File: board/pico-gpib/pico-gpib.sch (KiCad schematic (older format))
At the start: 37 parts, among them J2 USB_B_Micro, J3 RPI_GPIO, J4 Debug, U1 RP2040, U4 W25Q128JVS, U5 NCP1117-3.3, U6 CAT24C32, Y1 12M10PI/XT324-10/20

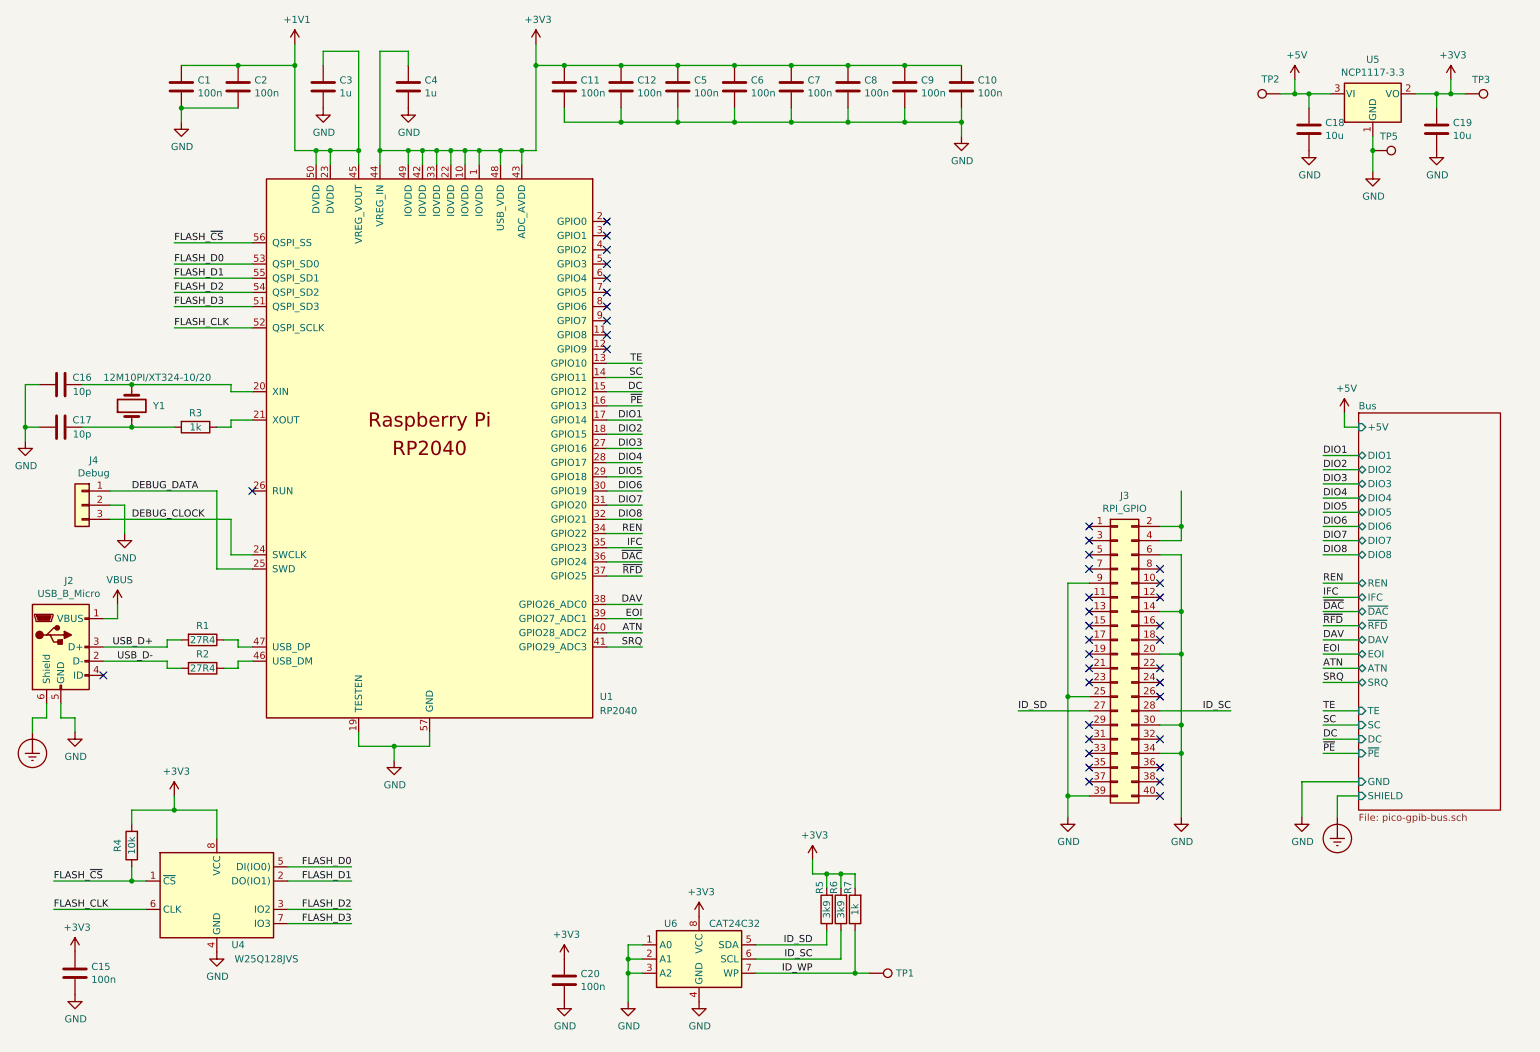
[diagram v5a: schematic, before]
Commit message: Renumber caps to make more sense.
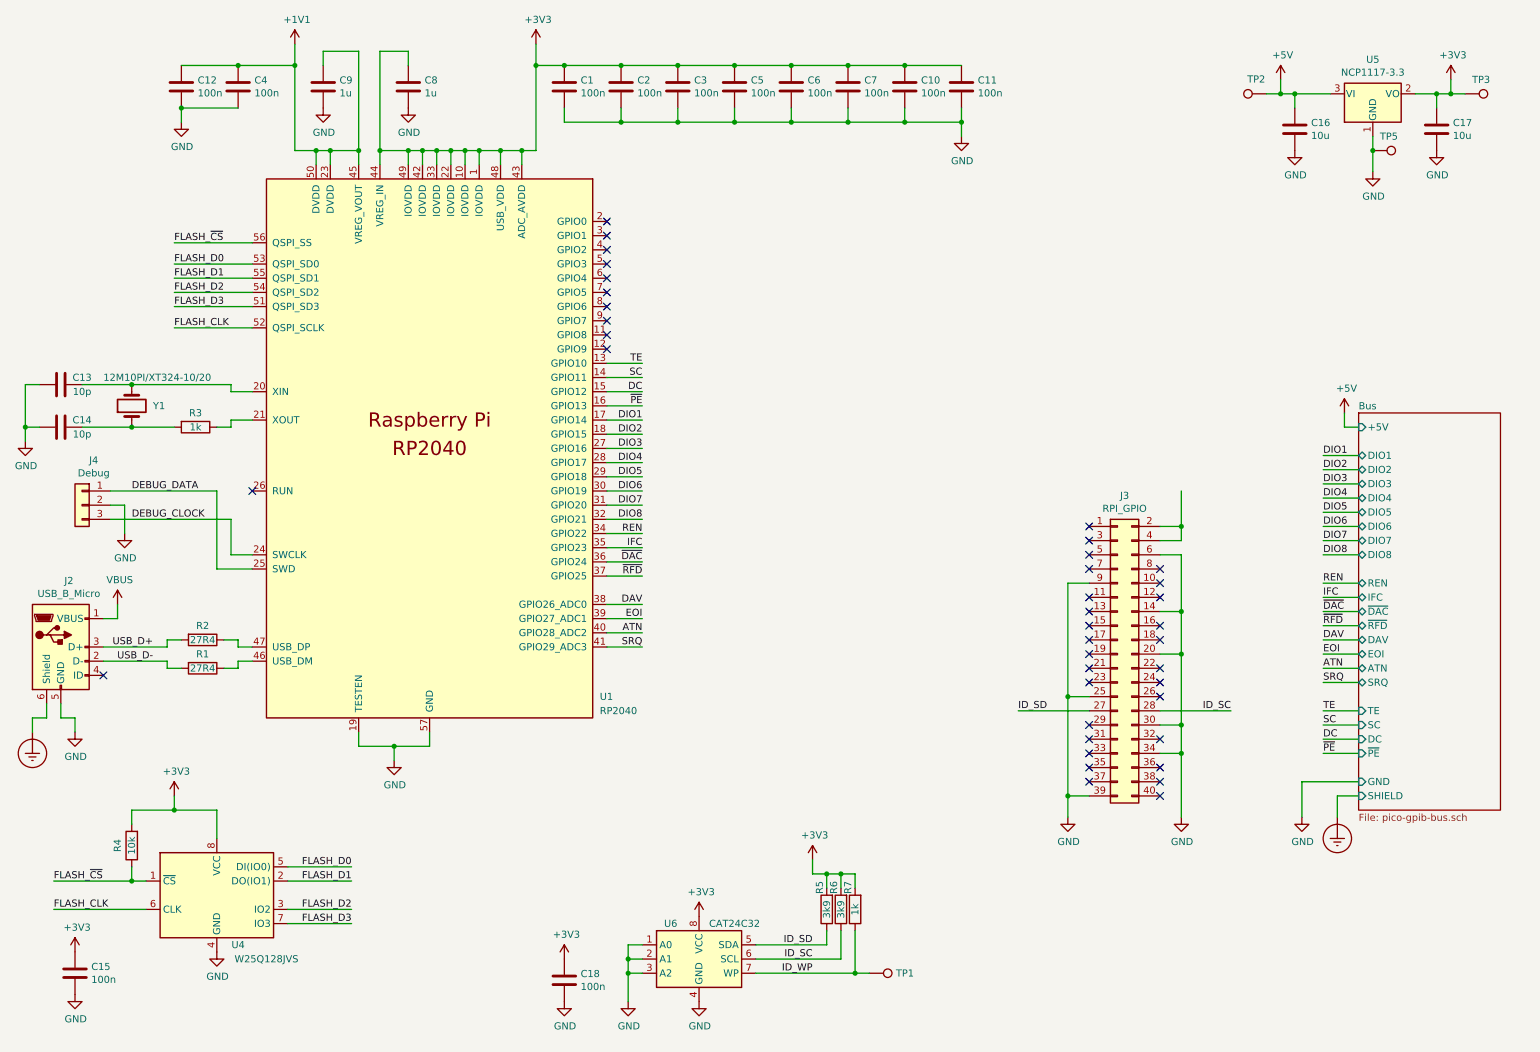
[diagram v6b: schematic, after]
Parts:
- renumbered C10 to C1, C6 to C10, C5 to C11, C1 to C12, C16 to C13, C17 to C14, C18 to C16, C19 to C17, C20 to C18, C8 to C2, C9 to C3, C2 to C4, C11 to C5, C12 to C6, C4 to C8, C3 to C9, R2 to R1, R1 to R2
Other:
- moved on the sheet: C1, C10, C11, C16, C2, C3, C5, C6, C7, TP2
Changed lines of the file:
@@
 ~PE
 $Comp
-L Device:C C4
+L Device:C C8
 U 1 1 625CDD18
 P 3300 1050
-F 0 "C4" H 3415 1096 50  0000 L CNN
+F 0 "C8" H 3415 1096 50  0000 L CNN
 F 1 "1u" H 3415 1005 50  0000 L CNN
 F 2 "Capacitor_SMD:C_0402_1005Metric" H 3338 900 50  0001 C CNN
@@
 $EndComp
 $Comp
-L Device:C C5
+L Device:C C11
 U 1 1 625CFFE4
-P 5200 1050
-F 0 "C5" H 5315 1096 50  0000 L CNN
-F 1 "100n" H 5315 1005 50  0000 L CNN
-F 2 "Capacitor_SMD:C_0402_1005Metric" H 5238 900 50  0001 C CNN
-F 3 "~" H 5200 1050 50  0001 C CNN
-	1    5200 1050
-	1    0    0    -1
-$EndComp
-$Comp
-L Device:C C6
+P 7200 1050
+F 0 "C11" H 7315 1096 50  0000 L CNN
+F 1 "100n" H 7315 1005 50  0000 L CNN
+F 2 "Capacitor_SMD:C_0402_1005Metric" H 7238 900 50  0001 C CNN
+F 3 "~" H 7200 1050 50  0001 C CNN
+	1    7200 1050
+	1    0    0    -1
+$EndComp
+$Comp
+L Device:C C10
 U 1 1 625D0C85
-P 5600 1050
-F 0 "C6" H 5715 1096 50  0000 L CNN
-F 1 "100n" H 5715 1005 50  0000 L CNN
-F 2 "Capacitor_SMD:C_0402_1005Metric" H 5638 900 50  0001 C CNN
-F 3 "~" H 5600 1050 50  0001 C CNN
-	1    5600 1050
-	1    0    0    -1
-$EndComp
-$Comp
-L Device:C C7
-U 1 1 625D1419
-P 6000 1050
-F 0 "C7" H 6115 1096 50  0000 L CNN
-F 1 "100n" H 6115 1005 50  0000 L CNN
-F 2 "Capacitor_SMD:C_0402_1005Metric" H 6038 900 50  0001 C CNN
-F 3 "~" H 6000 1050 50  0001 C CNN
-	1    6000 1050
-	1    0    0    -1
-$EndComp
-$Comp
-L Device:C C8
-U 1 1 625D1CD7
-P 6400 1050
-F 0 "C8" H 6515 1096 50  0000 L CNN
-F 1 "100n" H 6515 1005 50  0000 L CNN
-F 2 "Capacitor_SMD:C_0402_1005Metric" H 6438 900 50  0001 C CNN
-F 3 "~" H 6400 1050 50  0001 C CNN
-	1    6400 1050
-	1    0    0    -1
-$EndComp
-$Comp
-L Device:C C9
-U 1 1 625D225C
 P 6800 1050
-F 0 "C9" H 6915 1096 50  0000 L CNN
+F 0 "C10" H 6915 1096 50  0000 L CNN
 F 1 "100n" H 6915 1005 50  0000 L CNN
 F 2 "Capacitor_SMD:C_0402_1005Metric" H 6838 900 50  0001 C CNN
@@
 $EndComp
 $Comp
-L Device:C C10
+L Device:C C1
 U 1 1 625D27B5
-P 7200 1050
-F 0 "C10" H 7315 1096 50  0000 L CNN
-F 1 "100n" H 7315 1005 50  0000 L CNN
-F 2 "Capacitor_SMD:C_0402_1005Metric" H 7238 900 50  0001 C CNN
-F 3 "~" H 7200 1050 50  0001 C CNN
-	1    7200 1050
+P 4400 1050
+F 0 "C1" H 4515 1096 50  0000 L CNN
+F 1 "100n" H 4515 1005 50  0000 L CNN
+F 2 "Capacitor_SMD:C_0402_1005Metric" H 4438 900 50  0001 C CNN
+F 3 "~" H 4400 1050 50  0001 C CNN
+	1    4400 1050
 	1    0    0    -1
 $EndComp
@@
 $EndComp
 $Comp
-L Device:C C3
+L Device:C C9
 U 1 1 625F6CF0
 P 2700 1050
-F 0 "C3" H 2815 1096 50  0000 L CNN
+F 0 "C9" H 2815 1096 50  0000 L CNN
 F 1 "1u" H 2815 1005 50  0000 L CNN
 F 2 "Capacitor_SMD:C_0402_1005Metric" H 2738 900 50  0001 C CNN
@@
 $EndComp
 $Comp
-L Device:C C2
-U 1 1 625F79B4
-P 2100 1050
-F 0 "C2" H 2215 1096 50  0000 L CNN
-F 1 "100n" H 2215 1005 50  0000 L CNN
-F 2 "Capacitor_SMD:C_0402_1005Metric" H 2138 900 50  0001 C CNN
-F 3 "~" H 2100 1050 50  0001 C CNN
-	1    2100 1050
-	1    0    0    -1
-$EndComp
-$Comp
-L Device:C C1
+L Device:C C12
 U 1 1 625F8A02
 P 1700 1050
-F 0 "C1" H 1815 1096 50  0000 L CNN
+F 0 "C12" H 1815 1096 50  0000 L CNN
 F 1 "100n" H 1815 1005 50  0000 L CNN
 F 2 "Capacitor_SMD:C_0402_1005Metric" H 1738 900 50  0001 C CNN
@@
 $EndComp
 $Comp
-L Device:R R1
+L Device:R R2
 U 1 1 626338A8
 P 1850 4950
-F 0 "R1" V 1750 4950 50  0000 C CNN
+F 0 "R2" V 1750 4950 50  0000 C CNN
 F 1 "27R4" V 1850 4950 50  0000 C CNN
 F 2 "Resistor_SMD:R_0402_1005Metric" V 1780 4950 50  0001 C CNN
@@
 $EndComp
 $Comp
-L Device:R R2
+L Device:R R1
 U 1 1 62638F62
 P 1850 5150
-F 0 "R2" V 1750 5150 50  0000 C CNN
+F 0 "R1" V 1750 5150 50  0000 C CNN
 F 1 "27R4" V 1850 5150 50  0000 C CNN
 F 2 "Resistor_SMD:R_0402_1005Metric" V 1780 5150 50  0001 C CNN
@@
 Wire Wire Line
 	2100 900  2500 900
-$Comp
-L Device:C C12
-U 1 1 626DDD7A
-P 4800 1050
-F 0 "C12" H 4915 1096 50  0000 L CNN
-F 1 "100n" H 4915 1005 50  0000 L CNN
-F 2 "Capacitor_SMD:C_0402_1005Metric" H 4838 900 50  0001 C CNN
-F 3 "~" H 4800 1050 50  0001 C CNN
-	1    4800 1050
-	1    0    0    -1
-$EndComp
 Connection ~ 4800 900
 Wire Wire Line
 	4800 900  5200 900
-$Comp
-L Device:C C11
-U 1 1 626E7663
-P 4400 1050
-F 0 "C11" H 4515 1096 50  0000 L CNN
-F 1 "100n" H 4515 1005 50  0000 L CNN
-F 2 "Capacitor_SMD:C_0402_1005Metric" H 4438 900 50  0001 C CNN
-F 3 "~" H 4400 1050 50  0001 C CNN
-	1    4400 1050
-	1    0    0    -1
-$EndComp
 Connection ~ 4400 900
 Wire Wire Line
@@
 L power:GND #PWR0122
 U 1 1 628CC205
-P 9650 1500
-F 0 "#PWR0122" H 9650 1250 50  0001 C CNN
-F 1 "GND" H 9655 1327 50  0000 C CNN
-F 2 "" H 9650 1500 50  0001 C CNN
-F 3 "" H 9650 1500 50  0001 C CNN
-	1    9650 1500
-	1    0    0    -1
-$EndComp
-$Comp
-L Device:C C19
+P 9550 1500
+F 0 "#PWR0122" H 9550 1250 50  0001 C CNN
+F 1 "GND" H 9555 1327 50  0000 C CNN
+F 2 "" H 9550 1500 50  0001 C CNN
+F 3 "" H 9550 1500 50  0001 C CNN
+	1    9550 1500
+	1    0    0    -1
+$EndComp
+$Comp
+L Device:C C17
 U 1 1 628CC8FF
 P 10550 1350
-F 0 "C19" H 10665 1396 50  0000 L CNN
+F 0 "C17" H 10665 1396 50  0000 L CNN
 F 1 "10u" H 10665 1305 50  0000 L CNN
 F 2 "Capacitor_SMD:C_0402_1005Metric" H 10588 1200 50  0001 C CNN
@@
 $EndComp
 $Comp
-L Device:C C18
+L Device:C C16
 U 1 1 628CD260
-P 9650 1350
-F 0 "C18" H 9765 1396 50  0000 L CNN
-F 1 "10u" H 9765 1305 50  0000 L CNN
-F 2 "Capacitor_SMD:C_0402_1005Metric" H 9688 1200 50  0001 C CNN
-F 3 "~" H 9650 1350 50  0001 C CNN
-	1    9650 1350
+P 9550 1350
+F 0 "C16" H 9665 1396 50  0000 L CNN
+F 1 "10u" H 9665 1305 50  0000 L CNN
+F 2 "Capacitor_SMD:C_0402_1005Metric" H 9588 1200 50  0001 C CNN
+F 3 "~" H 9550 1350 50  0001 C CNN
+	1    9550 1350
 	1    0    0    -1
 $EndComp
@@
 	10550 1100 10550 1200
 Wire Wire Line
-	9800 1100 9650 1100
-Wire Wire Line
-	9650 1100 9650 1200
-Wire Wire Line
-	10100 1400 10100 1500
+	9800 1100 9550 1100
+Wire Wire Line
+	9550 1100 9550 1200
 $Comp
 L power:+3V3 #PWR0123
@@
 L power:+5V #PWR0124
 U 1 1 628F5D99
-P 9550 1000
-F 0 "#PWR0124" H 9550 850 50  0001 C CNN
-F 1 "+5V" H 9565 1173 50  0000 C CNN
-F 2 "" H 9550 1000 50  0001 C CNN
-F 3 "" H 9550 1000 50  0001 C CNN
-	1    9550 1000
-	1    0    0    -1
-$EndComp
-Wire Wire Line
-	9550 1000 9550 1100
-Wire Wire Line
-	9550 1100 9650 1100
-Connection ~ 9650 1100
+P 9450 1000
+F 0 "#PWR0124" H 9450 850 50  0001 C CNN
+F 1 "+5V" H 9465 1173 50  0000 C CNN
+F 2 "" H 9450 1000 50  0001 C CNN
+F 3 "" H 9450 1000 50  0001 C CNN
+	1    9450 1000
+	1    0    0    -1
+$EndComp
+Wire Wire Line
+	9450 1000 9450 1100
+Wire Wire Line
+	9450 1100 9550 1100
+Connection ~ 9550 1100
 Wire Wire Line
 	10550 1100 10650 1100
@@
 $EndComp
 $Comp
-L Device:C C16
+L Device:C C13
 U 1 1 62EE81B9
 P 850 3150
-F 0 "C16" V 800 3300 50  0000 C CNN
+F 0 "C13" V 800 3300 50  0000 C CNN
 F 1 "10p" V 900 3300 50  0000 C CNN
 F 2 "Capacitor_SMD:C_0402_1005Metric" H 888 3000 50  0001 C CNN
@@
 $EndComp
 $Comp
-L Device:C C17
+L Device:C C14
 U 1 1 62EE97F8
 P 850 3450
-F 0 "C17" V 800 3600 50  0000 C CNN
+F 0 "C14" V 800 3600 50  0000 C CNN
 F 1 "10p" V 900 3600 50  0000 C CNN
 F 2 "Capacitor_SMD:C_0402_1005Metric" H 888 3300 50  0001 C CNN
@@
 $EndComp
 $Comp
-L Device:C C20
+L Device:C C18
 U 1 1 634996B9
 P 4400 7350
-F 0 "C20" H 4515 7396 50  0000 L CNN
+F 0 "C18" H 4515 7396 50  0000 L CNN
 F 1 "100n" H 4515 7305 50  0000 L CNN
 F 2 "Capacitor_SMD:C_0402_1005Metric" H 4438 7200 50  0001 C CNN
@@
 NoConn ~ 2200 3900
 NoConn ~ 1150 5200
-Connection ~ 9550 1100
-Wire Wire Line
-	9450 1100 9550 1100
+Connection ~ 9450 1100
+Wire Wire Line
+	9350 1100 9450 1100
 $Comp
 L Connector:TestPoint TP2
 U 1 1 6374717A
-P 9450 1100
-F 0 "TP2" V 9553 1172 50  0000 C CNN
-F 1 "TestPoint" V 9554 1172 50  0001 C CNN
-F 2 "TestPoint:TestPoint_Pad_D1.0mm" H 9650 1100 50  0001 C CNN
-F 3 "~" H 9650 1100 50  0001 C CNN
-	1    9450 1100
+P 9350 1100
+F 0 "TP2" V 9453 1172 50  0000 C CNN
+F 1 "TestPoint" V 9454 1172 50  0001 C CNN
+F 2 "TestPoint:TestPoint_Pad_D1.0mm" H 9550 1100 50  0001 C CNN
+F 3 "~" H 9550 1100 50  0001 C CNN
+	1    9350 1100
 	0    -1   -1   0
 $EndComp
@@
 Connection ~ 10650 1100
 $Comp
+L Device:C C7
+U 1 1 625D1419
+P 6400 1050
+F 0 "C7" H 6515 1096 50  0000 L CNN
+F 1 "100n" H 6515 1005 50  0000 L CNN
+F 2 "Capacitor_SMD:C_0402_1005Metric" H 6438 900 50  0001 C CNN
+F 3 "~" H 6400 1050 50  0001 C CNN
+	1    6400 1050
+	1    0    0    -1
+$EndComp
+$Comp
+L Device:C C6
+U 1 1 626DDD7A
+P 6000 1050
+F 0 "C6" H 6115 1096 50  0000 L CNN
+F 1 "100n" H 6115 1005 50  0000 L CNN
+F 2 "Capacitor_SMD:C_0402_1005Metric" H 6038 900 50  0001 C CNN
+F 3 "~" H 6000 1050 50  0001 C CNN
+	1    6000 1050
+	1    0    0    -1
+$EndComp
+$Comp
+L Device:C C5
+U 1 1 626E7663
+P 5600 1050
+F 0 "C5" H 5715 1096 50  0000 L CNN
+F 1 "100n" H 5715 1005 50  0000 L CNN
+F 2 "Capacitor_SMD:C_0402_1005Metric" H 5638 900 50  0001 C CNN
+F 3 "~" H 5600 1050 50  0001 C CNN
+	1    5600 1050
+	1    0    0    -1
+$EndComp
+$Comp
+L Device:C C4
+U 1 1 625F79B4
+P 2100 1050
+F 0 "C4" H 2215 1096 50  0000 L CNN
+F 1 "100n" H 2215 1005 50  0000 L CNN
+F 2 "Capacitor_SMD:C_0402_1005Metric" H 2138 900 50  0001 C CNN
+F 3 "~" H 2100 1050 50  0001 C CNN
+	1    2100 1050
+	1    0    0    -1
+$EndComp
+$Comp
+L Device:C C3
+U 1 1 625D225C
+P 5200 1050
+F 0 "C3" H 5315 1096 50  0000 L CNN
+F 1 "100n" H 5315 1005 50  0000 L CNN
+F 2 "Capacitor_SMD:C_0402_1005Metric" H 5238 900 50  0001 C CNN
+F 3 "~" H 5200 1050 50  0001 C CNN
+	1    5200 1050
+	1    0    0    -1
+$EndComp
+$Comp
 L Connector:TestPoint TP5
 U 1 1 63801385
@@
 	0    1    1    0
 $EndComp
+Wire Wire Line
+	10100 1400 10100 1500
+Wire Wire Line
+	10100 1500 10100 1650
 Connection ~ 10100 1500
-Wire Wire Line
-	10100 1500 10100 1650
+$Comp
+L Device:C C2
+U 1 1 625D1CD7
+P 4800 1050
+F 0 "C2" H 4915 1096 50  0000 L CNN
+F 1 "100n" H 4915 1005 50  0000 L CNN
+F 2 "Capacitor_SMD:C_0402_1005Metric" H 4838 900 50  0001 C CNN
+F 3 "~" H 4800 1050 50  0001 C CNN
+	1    4800 1050
+	1    0    0    -1
+$EndComp
 $EndSCHEMATC

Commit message: Clean up pico schematic.
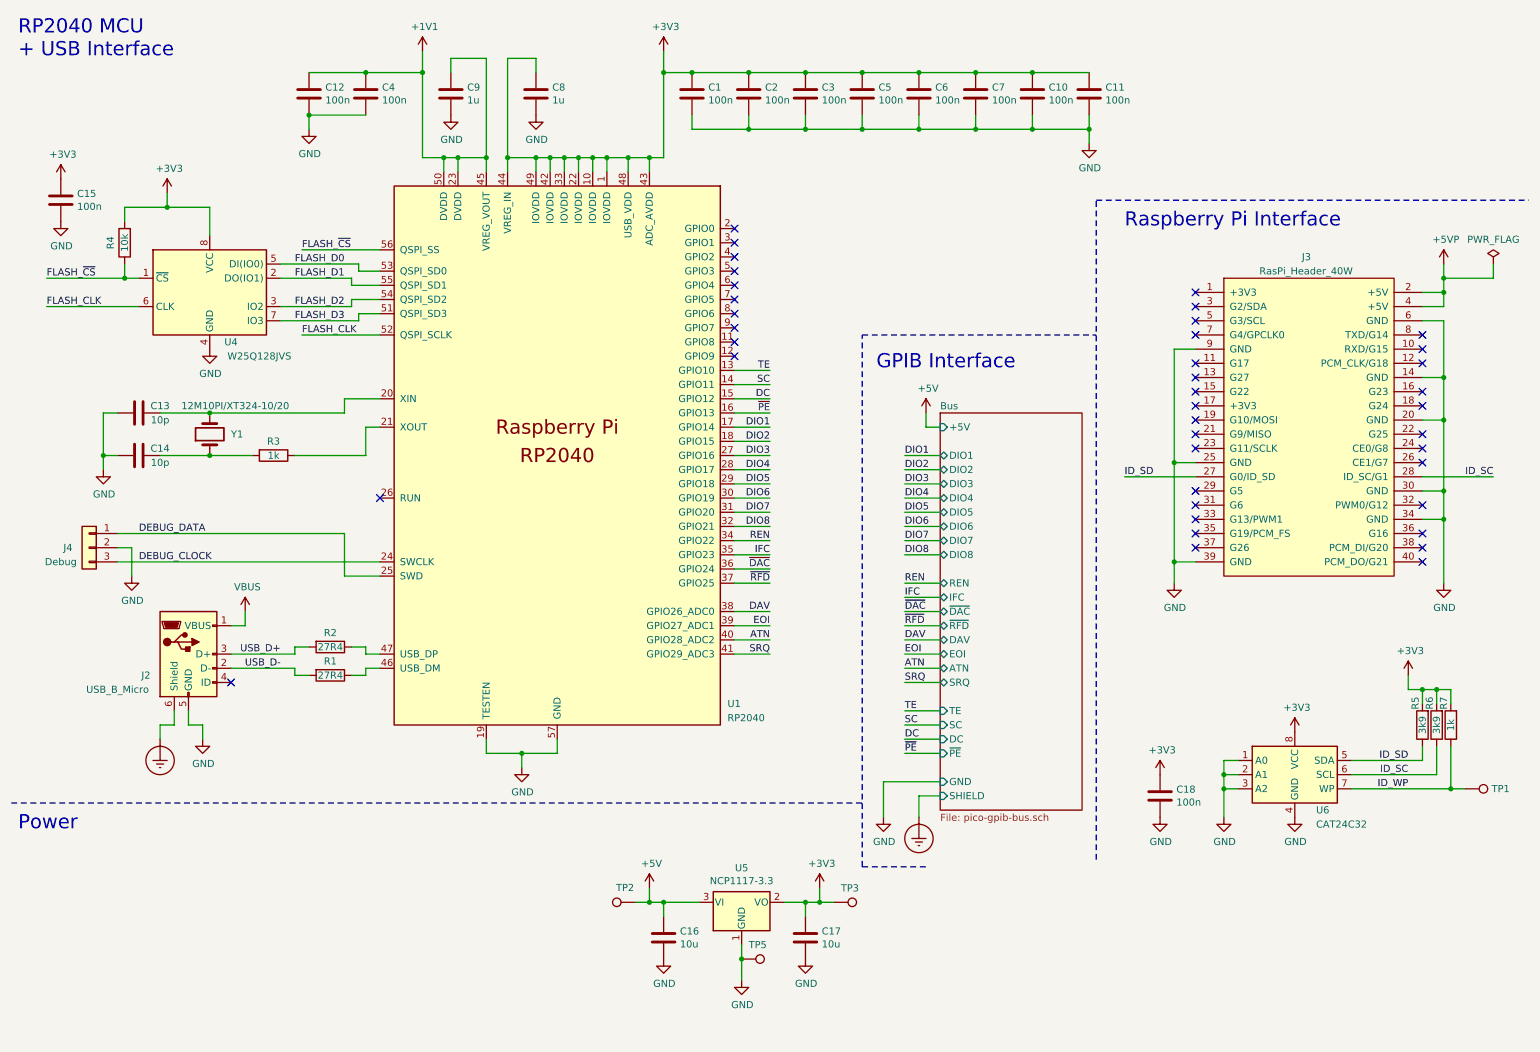
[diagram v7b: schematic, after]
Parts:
- removed J3: RPI_GPIO, lib:PinSocket_2x20_P2.54mm_Vertical_Centered_Anchor, symbol Connector_Generic:Conn_02x20_Odd_Even
- added J3: RasPi_Header_40W, local:PinSocket_2x20_P2.54mm_Vertical_Centered_Anchor, symbol local:RasPi_Header_40W
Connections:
- net GND: now also J3.14 (GND), J3.20 (GND), J3.25 (GND), J3.30 (GND), J3.34 (GND), J3.39 (GND), J3.6 (GND), J3.9 (GND)
- net ID_SC: now also J3.28 (ID_SC/G1)
- net ID_SD: now also J3.27 (G0/ID_SD)
- new net +5VP: J3.2 (+5V), J3.4 (+5V)
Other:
- note added: "GPIB Interface"
- note added: "Power"
- note added: "RP2040 MCU\n+ USB Interface"
- note added: "Raspberry Pi Interface"
- moved on the sheet: C1, C10, C11, C12, C13, C14, C15, C16, C17, C18, C2, C3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
